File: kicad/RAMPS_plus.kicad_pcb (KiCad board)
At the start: 2 copper layers, 120.7 x 66 mm, 136 parts, among them CON1 CON10, CON10 Stepstick_Left_Connector, CON11 Stepstick_Right_Connector, CON12 Stepstick_Left_Connector, CON13 Stepstick_Right_Connector, CON14 Stepstick_Left_Connector, CON15 Stepstick_Right_Connector, CON16 CON14x2, CON17 Stepstick_Left_Connector, CON18 Stepstick_Right_Connector, CON19 Stepstick_Left_Connector, CON2 CON8, CON20 Stepstick_Right_Connector, CON21 Panel1, CON22 Panel2, CON23 PS-ON, CON24 CON6, CON25 FAN, CON26 Chamber, CON27 BED, CON28 BED_Th, CON3 CON8, CON4 CON8, CON5 AUX, CON6 CON8, CON7 CON8, CON8 CON18x2, CON9 Carriage, Q1 IRLR2905ZPBF, Q2 IRLR2905ZPBF, Q3 FDC6401N, Q4 FDC6401N, Q5 IRLR2905ZPBF, Q6 FDC6401N, Q7 FDC6401N, Q8 FDC6401N, Q9 FDC6401N, SW1 RESET, U1 CD4504BPW, U2 SN74HCT245PW

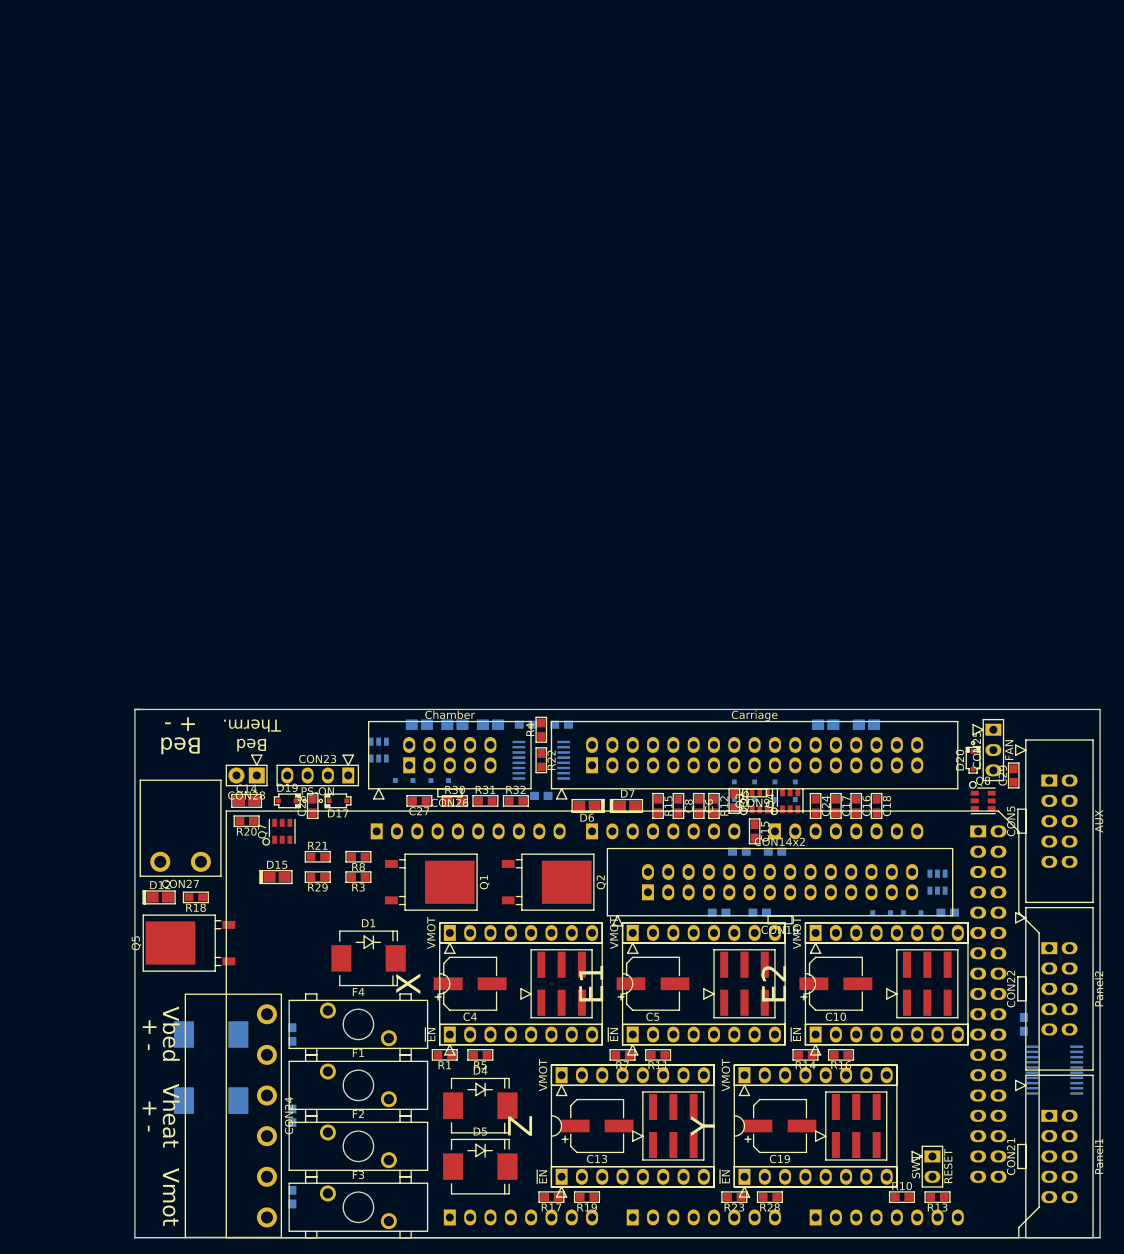
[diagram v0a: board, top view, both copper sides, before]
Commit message: Place. Add design rules (Merkar, 6/8mil)
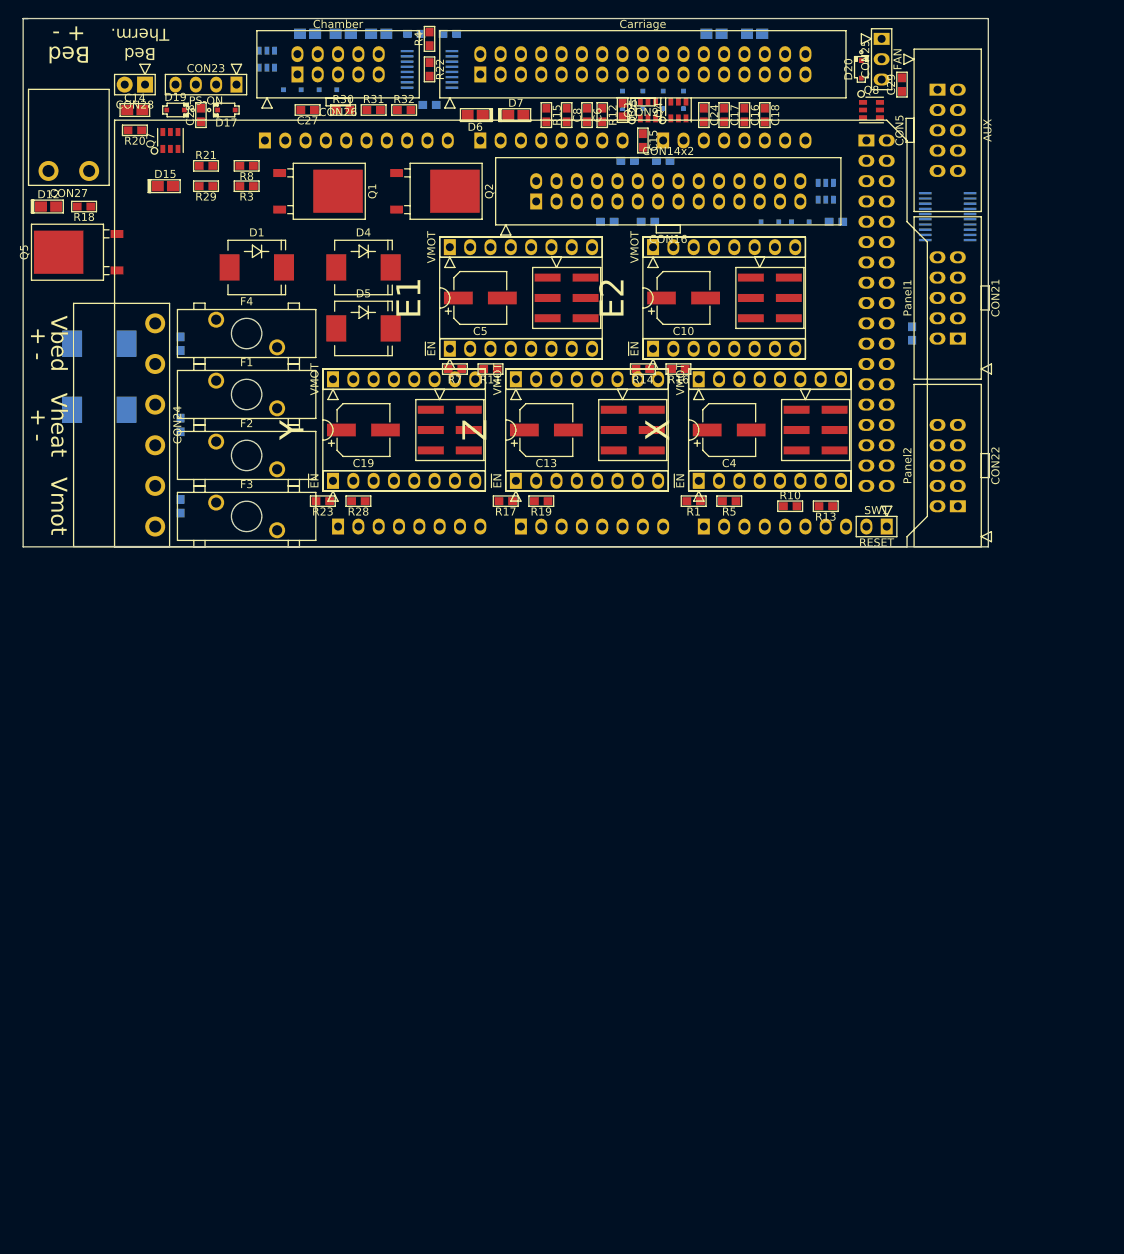
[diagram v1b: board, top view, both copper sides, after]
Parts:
- moved CON21 108.2 mm to (141.0, 60.3), turned to 90 degrees
- moved U2 107.5 mm to (141.0, 50.2), turned to 0 degrees
- moved D4 105.8 mm to (67.9, 56.5)
- moved D5 105.8 mm to (67.9, 64.1)
- moved C19 101.4 mm to (67.9, 76.8)
- moved CON19 101.1 mm to (73.0, 83.2)
- moved MECH6 101.1 mm to (73.0, 76.8)
- moved R23 101.1 mm to (62.9, 85.7)
- moved R28 101.1 mm to (67.3, 85.7)
- moved CON20 101.1 mm to (73.0, 70.5)
- moved JP5 100.7 mm to (78.7, 76.8), turned to 270 degrees
- moved CON12 88.7 mm to (87.6, 66.7)
- moved MECH3 88.7 mm to (87.6, 60.3)
- moved CON13 88.7 mm to (87.6, 54.0)
- moved JP2 88.6 mm to (93.3, 60.3), turned to 270 degrees
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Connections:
- CON21 pad 1: D37 -> +5V
- CON21 pad 10: +5V -> D37
- CON21 pad 2: D35 -> GND
- CON21 pad 3: /Panel/LCD_EN -> /Panel/LCD_D7
- CON21 pad 4: /Panel/LCD_RS -> /Panel/LCD_D6
- CON21 pad 5: /Panel/LCD_D4 -> /Panel/LCD_D5
- CON21 pad 6: /Panel/LCD_D5 -> /Panel/LCD_D4
- CON21 pad 7: /Panel/LCD_D6 -> /Panel/LCD_RS
- CON21 pad 8: /Panel/LCD_D7 -> /Panel/LCD_EN
- CON21 pad 9: GND -> D35
- CON22 pad 1: MISO -> (no net)
- CON22 pad 10: (no net) -> MISO
- CON22 pad 2: SCK -> (no net)
- CON22 pad 3: D31 -> D41
- CON22 pad 4: D53 -> D49
- CON22 pad 5: D33 -> MOSI
- CON22 pad 6: MOSI -> D33
- CON22 pad 7: D49 -> D53
- CON22 pad 8: D41 -> D31
- CON22 pad 9: (no net) -> SCK
- CON3 pad 4: (no net) -> A3
- CON3 pad 5: (no net) -> A4
- CON7 pad 7: D20 -> (no net)
- CON7 pad 8: D21 -> (no net)
- Q9 pad 1: D20 -> A3
- Q9 pad 3: D21 -> A4
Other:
- net class Default: clearance 0.254 -> 0.2032; trace_width 0.254 -> 0.1524; via_dia 0.889 -> 0.7; via_drill 0.635 -> 0.3
- rule trace_clearance: 0.254 -> 0.2032
- rule trace_min: 0.254 -> 0.1524
- rule via_min_drill: 0.508 -> 0.3
- rule via_min_size: 0.889 -> 0.7

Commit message: Start routing.
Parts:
- moved R23 1.80 mm to (64.1, 87.0)
- moved R1 1.42 mm to (109.9, 87.0)
- moved R10 1.42 mm to (122.6, 87.0)
- moved R17 1.42 mm to (86.4, 87.0)
- moved R28 1.42 mm to (67.9, 87.0)
- moved C13 1.27 mm to (90.8, 78.1)
- moved C19 1.27 mm to (67.9, 78.1)
- moved C4 1.27 mm to (113.7, 78.1)
- moved JP1 1.27 mm to (124.5, 78.1)
- moved JP4 1.27 mm to (101.6, 78.1)
- moved JP5 1.27 mm to (78.7, 78.1)
- moved MECH2 1.27 mm to (118.7, 78.1)
- moved MECH5 1.27 mm to (95.9, 78.1)
- moved MECH6 1.27 mm to (73.0, 78.1)
- moved R19 1.27 mm to (90.2, 87.0)
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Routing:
- net IOREF: track 0.00 -> 48.5 mm
- net SCK: track 0.00 -> 26.7 mm
- net D31: track 0.00 -> 26.5 mm
- net D33: track 0.00 -> 26.5 mm
- net D41: track 0.00 -> 21.2 mm
- net Net-(CON19-Pad2): track 0.00 -> 19.4 mm
- net Net-(CON12-Pad2): track 0.00 -> 17.9 mm
- net D53: track 0.00 -> 17.6 mm
- net Net-(CON10-Pad2): track 0.00 -> 17.3 mm
- net Net-(CON14-Pad2): track 0.00 -> 17.1 mm
- net Net-(CON17-Pad2): track 0.00 -> 17.1 mm
- net D36: track 0.00 -> 14.4 mm
- net D34: track 0.00 -> 12.1 mm
- net Net-(CON12-Pad3): track 0.00 -> 10.5 mm
- net Net-(CON19-Pad3): track 0.00 -> 10.5 mm
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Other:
- outline, holes or cut-outs redrawn

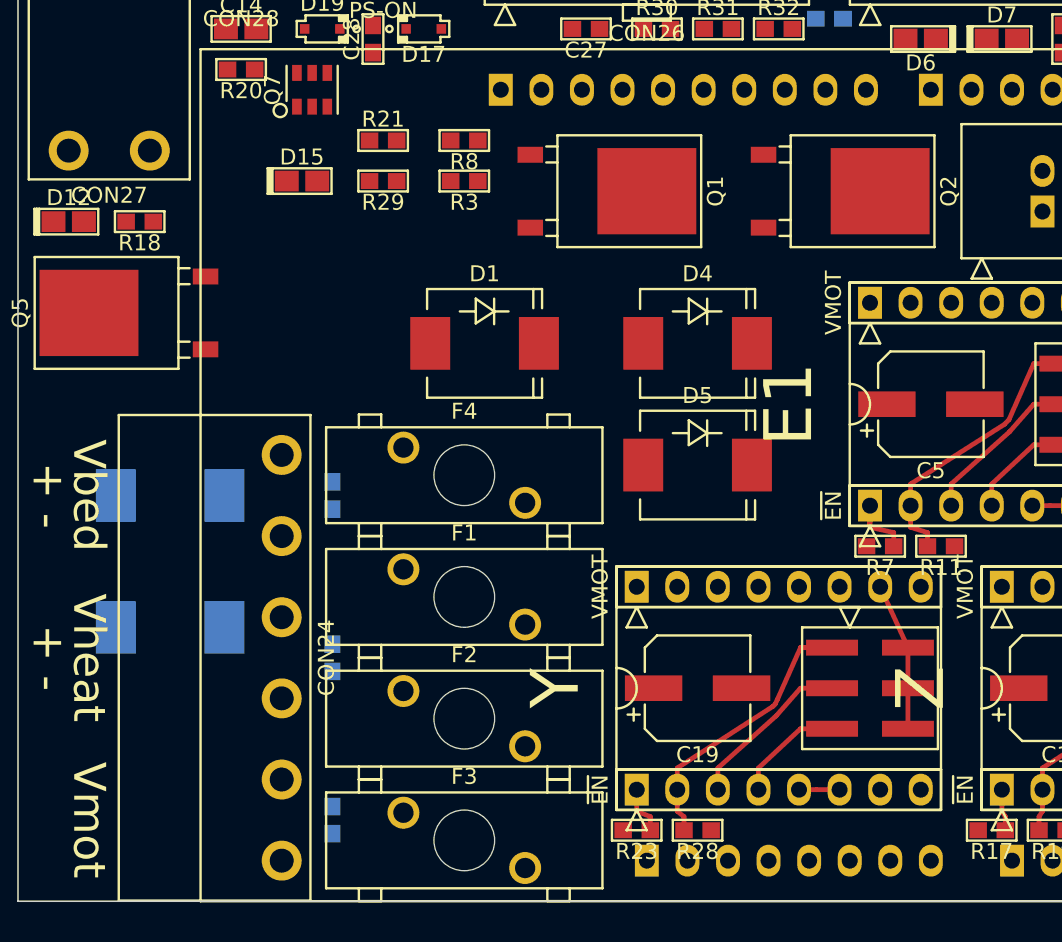
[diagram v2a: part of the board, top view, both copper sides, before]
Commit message: Delete fuse on +12V. Chcange fuse & diode placement.
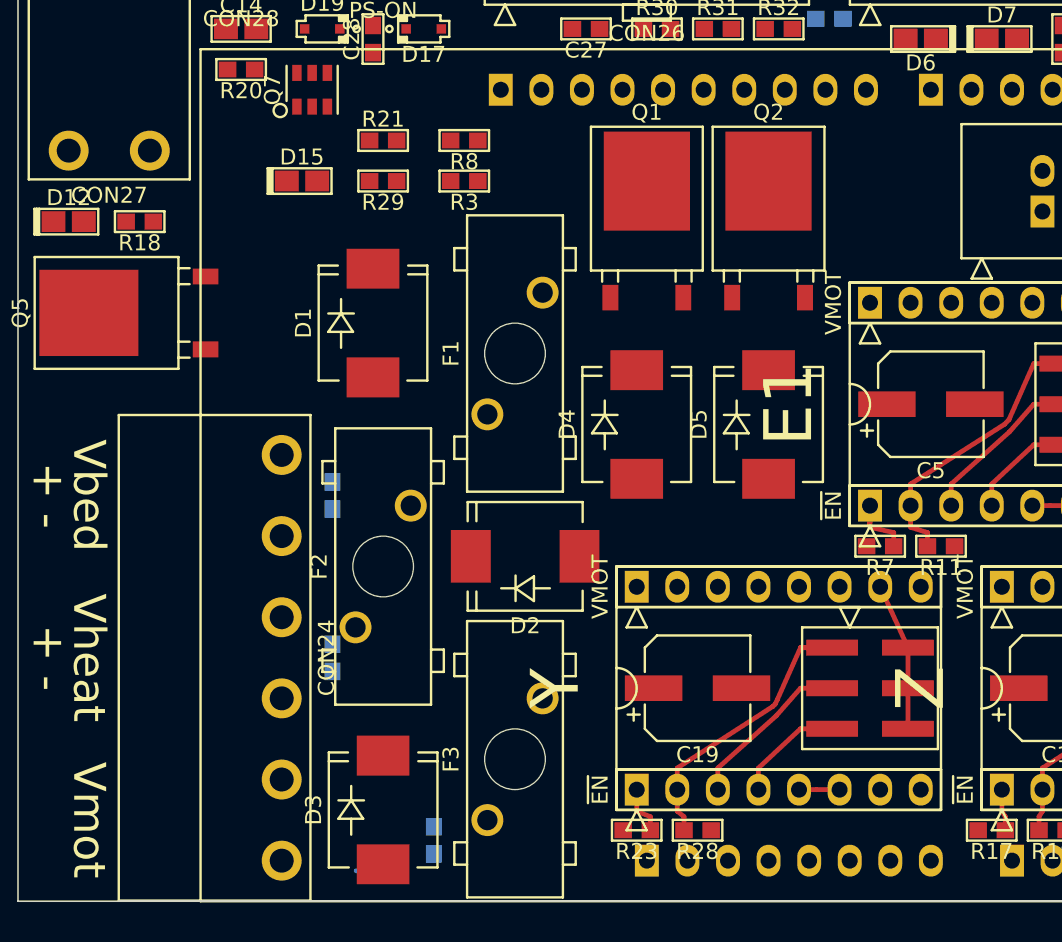
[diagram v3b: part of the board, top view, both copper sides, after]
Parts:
- removed F4: MINI_Blade_Fuse_Holder, pnConnector:Littlefuse_01530008
- D2, D3: moved to F.Cu
- moved D3 23.8 mm to (48.3, 85.7), turned to 90 degrees
- moved D2 22.7 mm to (57.1, 69.8)
- moved F1 15.6 mm to (56.5, 57.1), turned to 90 degrees
- moved F2 10.8 mm to (48.3, 70.5), turned to 90 degrees
- moved D1 7.10 mm to (47.6, 55.2), turned to 90 degrees
- moved Q2 7.01 mm to (72.4, 46.4), turned to 0 degrees
- moved C3 6.48 mm to (51.4, 87.6)
- moved D4 6.35 mm to (64.1, 61.6), turned to 90 degrees
- moved F3 5.99 mm to (56.5, 82.5), turned to 90 degrees
- moved D5 5.12 mm to (72.4, 61.6), turned to 90 degrees
- moved Q1 0.64 mm to (64.8, 46.4), turned to 0 degrees
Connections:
- D4 pad 1: Net-(D4-Pad1) -> +12V
- D4 pad 2: Net-(C2-Pad1) -> Vheat
- D5 pad 1: Net-(D4-Pad1) -> +12V
- D5 pad 2: Net-(C3-Pad1) -> Vmot
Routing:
- net (no net): track 0.00 -> 0.93 mm

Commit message: Route.
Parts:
- moved D12 4.33 mm to (32.9, 49.3)
- moved R18 3.44 mm to (36.4, 48.6), turned to 270 degrees
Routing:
- net IOREF: track 48.5 -> 96.4 mm
- net A0: track 0.00 -> 44.5 mm, vias 0 -> 1
- net A1: track 0.00 -> 43.0 mm, vias 0 -> 1
- net A15: track 0.00 -> 41.3 mm
- net D46: track 0.00 -> 40.9 mm
- net D48: track 0.00 -> 36.5 mm
- net A2: track 3.12 -> 35.9 mm
- net A11: track 0.00 -> 31.5 mm
- net A6: track 0.00 -> 27.4 mm
- net A10: track 0.00 -> 26.7 mm
- net A9: track 0.00 -> 26.6 mm
- net A7: track 0.00 -> 26.6 mm
- net Net-(C3-Pad1): track 0.00 -> 13.5 mm
- net Net-(C1-Pad1): track 0.00 -> 13.1 mm
- net Vmot: track 0.00 -> 11.1 mm
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
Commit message: Route.
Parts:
- moved D7 13.2 mm to (78.6, 47.7), turned to 180 degrees
- moved R2 13.2 mm to (78.6, 47.7), turned to 0 degrees
- moved D6 8.61 mm to (78.8, 45.5)
- moved R6 8.61 mm to (78.8, 45.5)
- moved R15 1.10 mm to (91.9, 37.5)
- moved C8 0.48 mm to (93.8, 37.5)
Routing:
- net /Carriage/XmotorB: track 0.00 -> 46.3 mm
- net /Carriage/XmotorA: track 0.00 -> 45.0 mm
- net /Carriage/XmotorD: track 0.00 -> 43.3 mm
- net /YZ axis/YmotorD: track 0.00 -> 42.2 mm
- net /Carriage/XmotorC: track 0.00 -> 41.8 mm
- net /YZ axis/ZmotorB: track 0.00 -> 41.5 mm
- net /YZ axis/ZmotorD: track 0.00 -> 40.6 mm
- net /YZ axis/ZmotorA: track 0.00 -> 40.4 mm, vias 0 -> 1
- net /YZ axis/YmotorB: track 0.00 -> 40.0 mm
- net /Carriage/E1MotorD: track 0.00 -> 38.2 mm, vias 0 -> 1
- net /YZ axis/ZmotorC: track 0.00 -> 37.8 mm
- net /YZ axis/YmotorA: track 0.00 -> 37.4 mm
- net /YZ axis/YmotorC: track 0.00 -> 36.4 mm
- net /Carriage/E1MotorB: track 0.00 -> 35.5 mm, vias 0 -> 1
- net /Carriage/E1MotorC: track 0.00 -> 33.5 mm, vias 0 -> 1
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
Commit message: Route.
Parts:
- moved C20 12.0 mm to (144.8, 56.0), turned to 90 degrees
- moved U2 1.08 mm to (140.2, 49.4)
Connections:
- U2 pad 13: /Panel/LCD_D7 -> /Panel/LCD_D4
- U2 pad 14: /Panel/LCD_D6 -> /Panel/LCD_D5
- U2 pad 15: /Panel/LCD_D5 -> /Panel/LCD_D6
- U2 pad 16: /Panel/LCD_D4 -> /Panel/LCD_D7
- U2 pad 4: D23 -> D29
- U2 pad 5: D25 -> D27
- U2 pad 6: D27 -> D25
- U2 pad 7: D29 -> D23
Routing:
- net D39: track 0.00 -> 33.1 mm
- net D42: track 0.00 -> 32.4 mm
- net D43: track 0.00 -> 31.2 mm
- net D44: track 0.00 -> 30.4 mm, vias 0 -> 1
- net D40: track 0.00 -> 29.5 mm
- net D32: track 0.00 -> 27.1 mm
- net +12V: track 0.00 -> 13.0 mm
- net GND: track 7.37 -> 19.2 mm
- net A13: track 3.08 -> 8.99 mm
- net D15: track 0.00 -> 5.69 mm
- net Net-(CON25-Pad3): track 0.00 -> 5.41 mm
- net D14: track 0.00 -> 2.68 mm
- net A14: track 3.08 -> 5.64 mm
- net D19: track 0.00 -> 2.33 mm
- net D18: track 0.00 -> 2.33 mm

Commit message: Route.
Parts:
- moved R20 102.5 mm to (130.1, 87.0)
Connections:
- CON5 pad 1: D32 -> D42
- CON5 pad 3: D39 -> D43
- CON5 pad 7: D42 -> D39
- CON5 pad 9: D43 -> D32
- Q6 pad 1: D44 -> D45
- Q6 pad 3: D45 -> D44
- Q6 pad 4: /YZ axis/OC6 -> /YZ axis/OC5
- Q6 pad 6: /YZ axis/OC5 -> /YZ axis/OC6
- Q9 pad 1: A3 -> A4
- Q9 pad 3: A4 -> A3
- Q9 pad 4: /Power/Chamber-fan -> /Power/Chamber-heater
- Q9 pad 6: /Power/Chamber-heater -> /Power/Chamber-fan
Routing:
- net GND: track 19.2 -> 128.9 mm, vias 4 -> 14
- net Vmot: track 11.1 -> 120.5 mm, vias 0 -> 6
- net D47: track 0.00 -> 41.5 mm
- net +12V: track 13.0 -> 52.2 mm
- net D45: track 0.00 -> 29.4 mm, vias 0 -> 1
- net /Panel/LCD_D7: track 0.00 -> 21.8 mm, vias 0 -> 1
- net /Panel/LCD_D6: track 0.00 -> 18.9 mm, vias 0 -> 1
- net /Panel/LCD_D4: track 0.00 -> 17.5 mm, vias 0 -> 1
- net /Panel/LCD_D5: track 0.00 -> 14.0 mm, vias 0 -> 1
- net /Power/PS-ON: track 0.00 -> 13.0 mm
- net A9: track 26.6 -> 39.1 mm
- net /Power/Chamber-fan: track 0.00 -> 12.0 mm
- net Vheat: track 4.92 -> 16.4 mm
- net A11: track 31.5 -> 42.3 mm
- net D35: track 0.00 -> 10.8 mm
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
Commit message: Route.
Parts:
- moved R8 6.17 mm to (59.4, 45.0), turned to 90 degrees
- moved R3 4.20 mm to (57.3, 45.0), turned to 90 degrees
- moved C10 2.69 mm to (105.3, 60.2)
- moved JP3 1.28 mm to (117.5, 60.4)
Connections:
- CON8 pad 1: 5V -> +5V
- CON8 pad 2: 5V -> +5V
- U2 pad 11: (no net) -> /Panel/LCD_EN
- U2 pad 12: (no net) -> /Panel/LCD_RS
- U2 pad 17: /Panel/LCD_RS -> (no net)
- U2 pad 18: /Panel/LCD_EN -> (no net)
- U2 pad 2: D17 -> +5V
- U2 pad 3: D16 -> +5V
- U2 pad 8: GND -> D16
- U2 pad 9: GND -> D17
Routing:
- net D24: track 4.50 -> 76.5 mm, vias 0 -> 3
- net +12V: track 52.2 -> 111.7 mm
- net D26: track 0.00 -> 45.1 mm, vias 0 -> 2
- net D28: track 0.00 -> 40.8 mm, vias 0 -> 2
- net D16: track 0.00 -> 32.3 mm, vias 0 -> 1
- net D30: track 2.60 -> 34.7 mm, vias 0 -> 1
- net D17: track 0.00 -> 28.7 mm, vias 0 -> 1
- net Net-(Q2-Pad1): track 0.00 -> 14.1 mm
- net GND: track 128.9 -> 116.0 mm
- net IOREF: track 107.0 -> 118.2 mm
- net /YZ axis/OC5: track 2.56 -> 12.8 mm
- net /Panel/LCD_EN: track 10.1 -> 0.00 mm, vias 1 -> 0
- net Net-(Q1-Pad1): track 0.00 -> 9.81 mm
- net D45: track 29.4 -> 34.5 mm
- net /YZ axis/OC6: track 3.18 -> 6.92 mm
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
